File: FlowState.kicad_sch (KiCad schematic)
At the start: 13 parts, among them J1 USB_C_Receptacle_USB2.0_16P, J2 Conn_01x04_Pin (CO2), J3 Conn_01x14_Pin(LCD), J4 Conn_01x03_Pin (SOIL), J5 Conn_01x04_Pin(SD), J6 Conn_01x02_Pin(Switch), U1 AMS1117-3.3, U2 ESP32-DEVKIT-V1

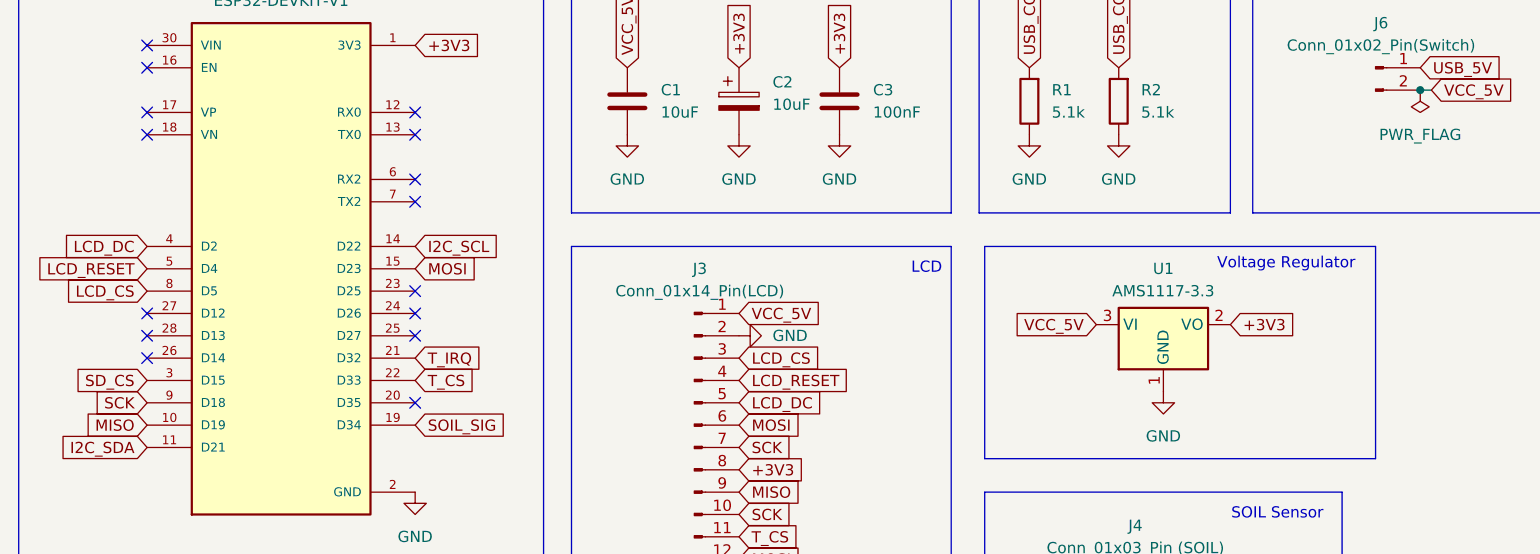
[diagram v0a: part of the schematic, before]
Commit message: edits
rewired LCD to differnt GPIO because that pin has HIGH voltage at startup
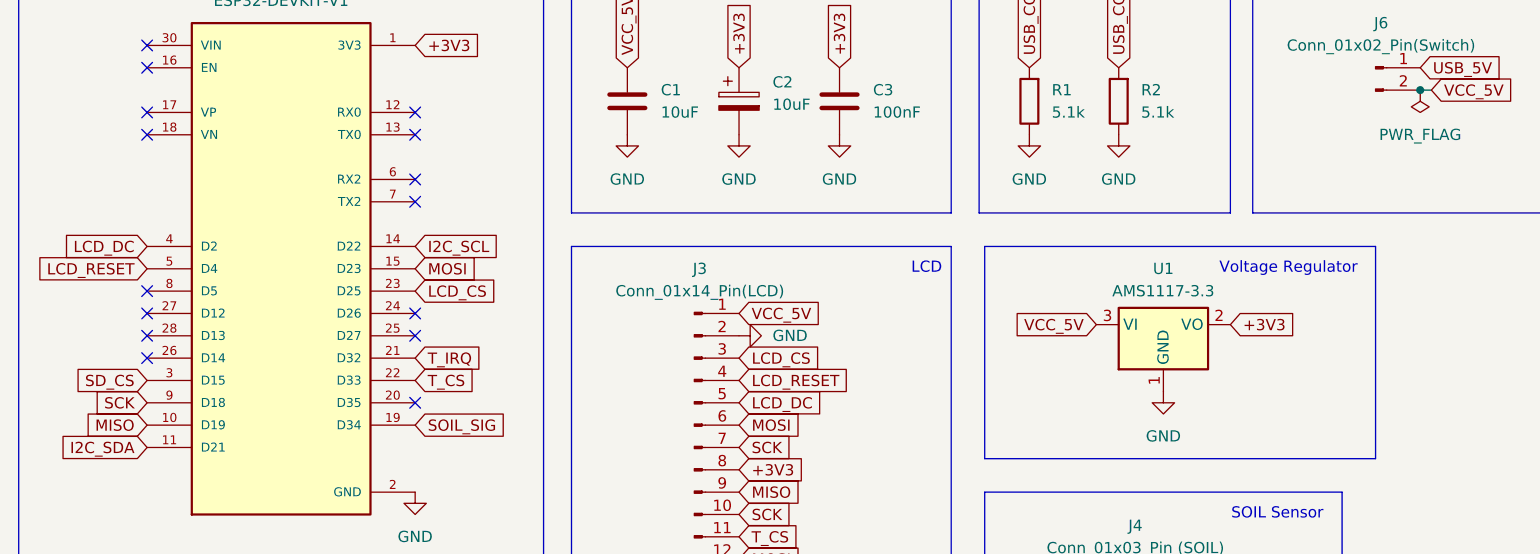
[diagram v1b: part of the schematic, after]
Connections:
- net LCD_CS: now also U2.23 (D25); no longer U2.8 (D5)
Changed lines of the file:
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@@
 	(text "Voltage Regulator\n"
 		(exclude_from_sim no)
-		(at 163.83 51.562 0)
+		(at 164.084 52.07 0)
 		(effects
 			(font
@@
 	)
 	(no_connect
-		(at 64.77 54.61)
-	)
-	(no_connect
 		(at 34.29 59.69)
 	)
@@
 	(no_connect
 		(at 63.5 114.3)
+	)
+	(no_connect
+		(at 34.29 54.61)
 	)
 	(no_connect
@@
 		)
 	)
+	(global_label "LCD_CS"
+		(shape input)
+		(at 64.77 54.61 0)
+		(fields_autoplaced yes)
+		(effects
+			(font
+				(size 1.27 1.27)
+			)
+			(justify left)
+		)
+		(property "Intersheetrefs" "${INTERSHEET_REFS}"
+			(at 74.7704 54.61 0)
+			(effects
+				(font
+					(size 1.27 1.27)
+				)
+				(justify left)
+				(hide yes)
+			)
+		)
+	)
 	(global_label "MISO"
 		(shape input)
@@
 			(effects
 				(font
-					(size 1.27 1.27)
-				)
-				(justify right)
-				(hide yes)
-			)
-		)
-	)
-	(global_label "LCD_CS"
-		(shape input)
-		(at 34.29 54.61 180)
-		(fields_autoplaced yes)
-		(effects
-			(font
-				(size 1.27 1.27)
-			)
-			(justify right)
-		)
-		(property "Intersheetrefs" "${INTERSHEET_REFS}"
-			(at 24.2896 54.61 0)
-			(effects
-				(font

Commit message: heatsink
heatsink good now
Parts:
- C2: value 10uF -> 47uF
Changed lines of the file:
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@@
 			)
 		)
-		(property "Value" "10uF"
+		(property "Value" "47uF"
 			(at 105.41 33.4009 0)
 			(effects

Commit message: gerber, step, readme
did lots of stuff
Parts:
- added D1: 1N5819, Diode_THT:D_DO-41_SOD81_P10.16mm_Horizontal, symbol Diode:1N5819
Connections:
- net USB_5V: now also D1.2 (A)
- net VCC_5V: now also D1.1 (K)
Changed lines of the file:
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@@
+	)
+	(rectangle
+		(start 197.612 16.51)
+		(end 215.9 45.466)
+		(stroke
+			(width 0)
+			(type default)
+		)
+		(fill
+			(type none)
+		)
 	)
 	(rectangle
@@
 		)
 	)
+	(global_label "USB_5V"
+		(shape input)
+		(at 210.82 31.75 270)
+		(fields_autoplaced yes)
+		(effects
+			(font
+				(size 1.27 1.27)
+			)
+			(justify right)
+		)
+		(property "Intersheetrefs" "${INTERSHEET_REFS}"
+			(at 210.82 41.8109 90)
+			(effects
+				(font
+					(size 1.27 1.27)
+				)
+				(justify right)
+				(hide yes)
+			)
+		)
+	)
 	(global_label "SCK"
 		(shape input)
@@
 				)
 				(justify left)
+				(hide yes)
+			)
+		)
+	)
+	(global_label "VCC_5V"
+		(shape input)
+		(at 203.2 31.75 270)
+		(fields_autoplaced yes)
+		(effects
+			(font
+				(size 1.27 1.27)
+			)
+			(justify right)
+		)
+		(property "Intersheetrefs" "${INTERSHEET_REFS}"
+			(at 203.2 41.6295 90)
+			(effects
+				(font
+					(size 1.27 1.27)
+				)
+				(justify right)
 				(hide yes)
 			)
@@
 					(unit 1)
 				)
+			)
+		)
+	)
+	(symbol
+		(lib_id "Diode:1N5819")
+		(at 207.01 31.75 0)
+		(unit 1)
+		(exclude_from_sim no)
+		(in_bom yes)
+		(on_board yes)
+		(dnp no)
+		(fields_autoplaced yes)
+		(property "Reference" "D1"
+			(at 206.6925 25.4 0)
+			(effects
+				(font
+					(size 1.27 1.27)
+				)
+			)
+		)
+		(property "Value" "1N5819"
+			(at 206.6925 27.94 0)
+			(effects
+				(font
+					(size 1.27 1.27)
+				)
+			)
+		)
+		(property "Footprint" "Diode_THT:D_DO-41_SOD81_P10.16mm_Horizontal"
+			(at 207.01 36.195 0)
+			(effects
+				(font
+					(size 1.27 1.27)
+				)
+				(hide yes)
+			)
+		)
+		(property "Datasheet" "http://www.vishay.com/docs/88525/1n5817.pdf"
+			(at 207.01 31.75 0)
+			(effects
+				(font
+					(size 1.27 1.27)
+				)
+				(hide yes)
+			)
+		)
+		(property "Description" "40V 1A Schottky Barrier Rectifier Diode, DO-41"
+			(at 207.01 31.75 0)
+			(effects
+				(font
+					(size 1.27 1.27)
+				)
+				(hide yes)
+			)
+		)
+		(pin "2"
+		)
+		(pin "1"
+		)
+		(instances
+			(project "FlowState"
+				(path "/cfffbc31-3f87-49bc-9bca-b04c0605b8f9"
+					(reference "D1")
+					(unit 1)
+				)
